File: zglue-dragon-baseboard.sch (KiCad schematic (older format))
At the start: 7 parts, among them U1 zGlue-Dragon

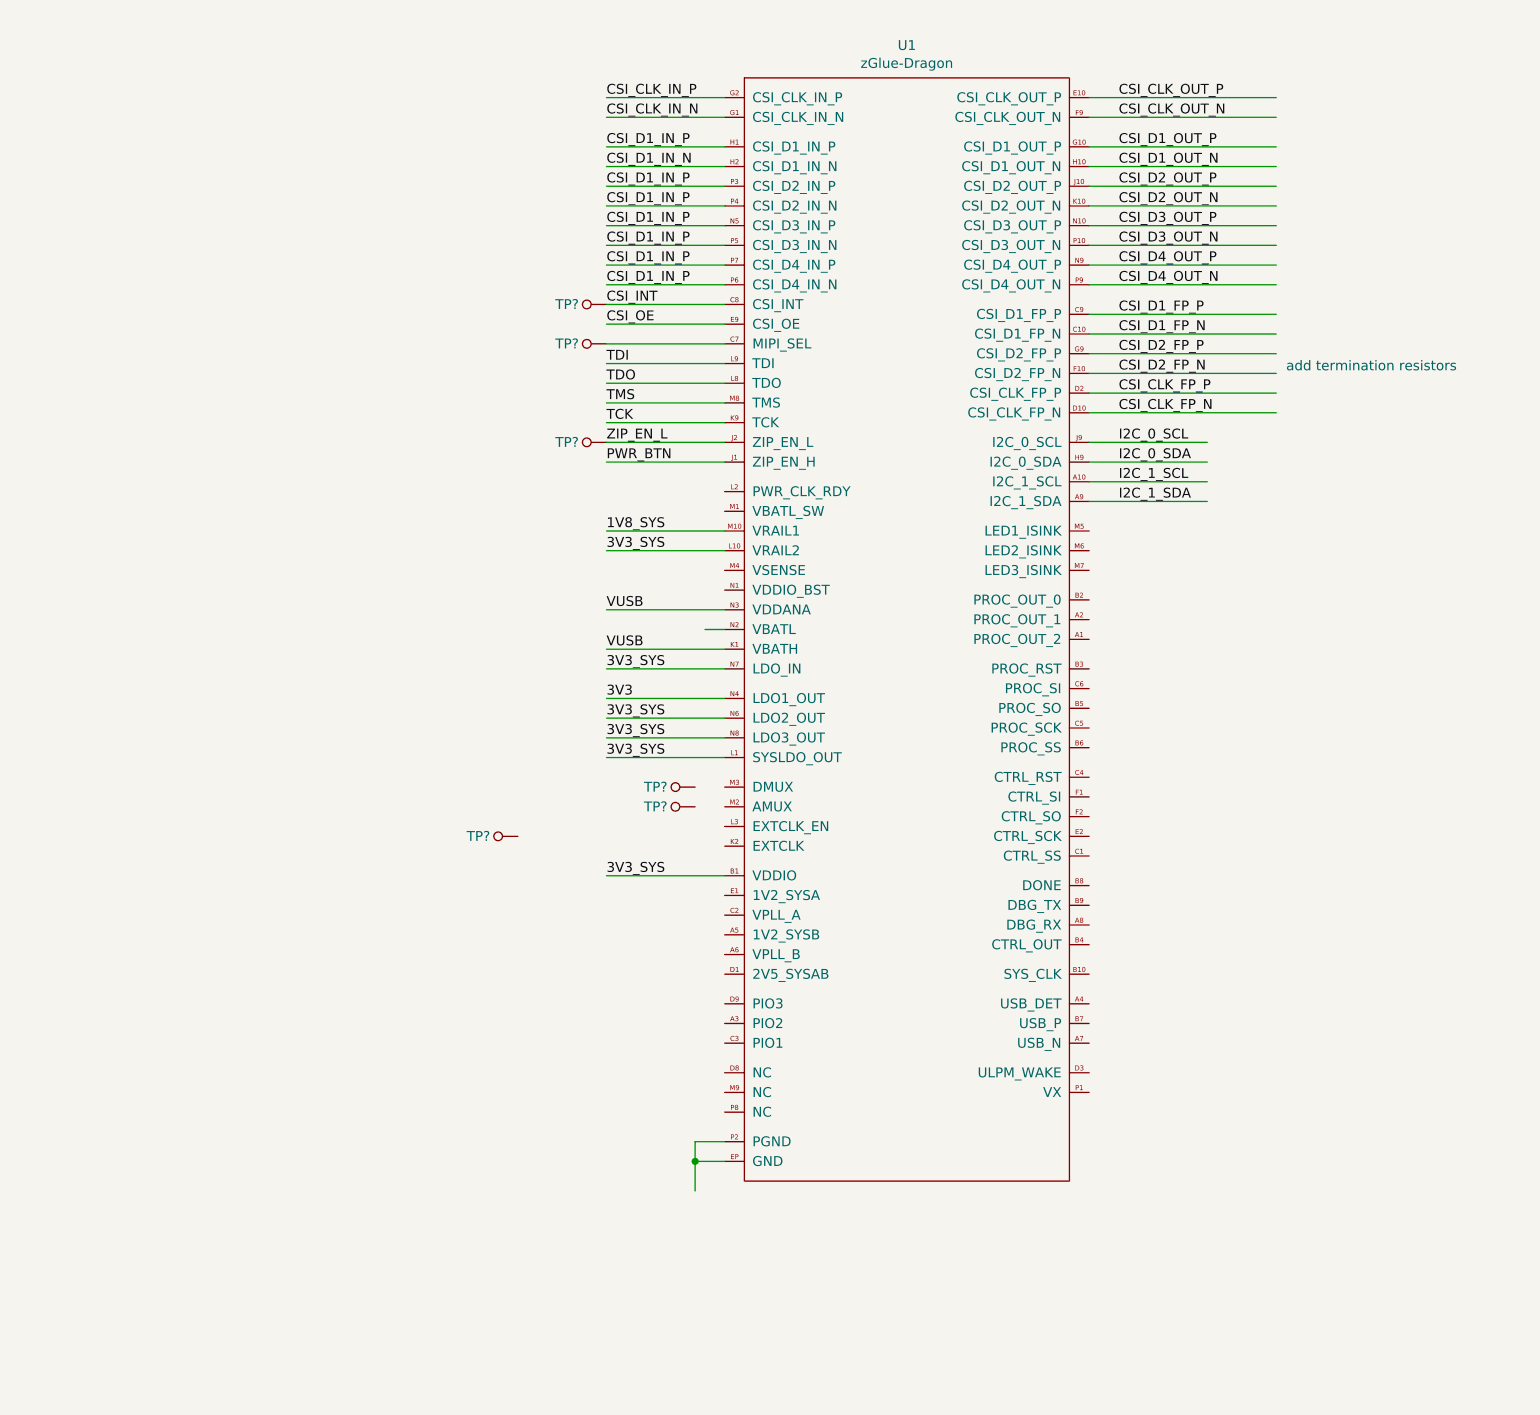
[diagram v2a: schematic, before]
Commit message: Added MIPI termination
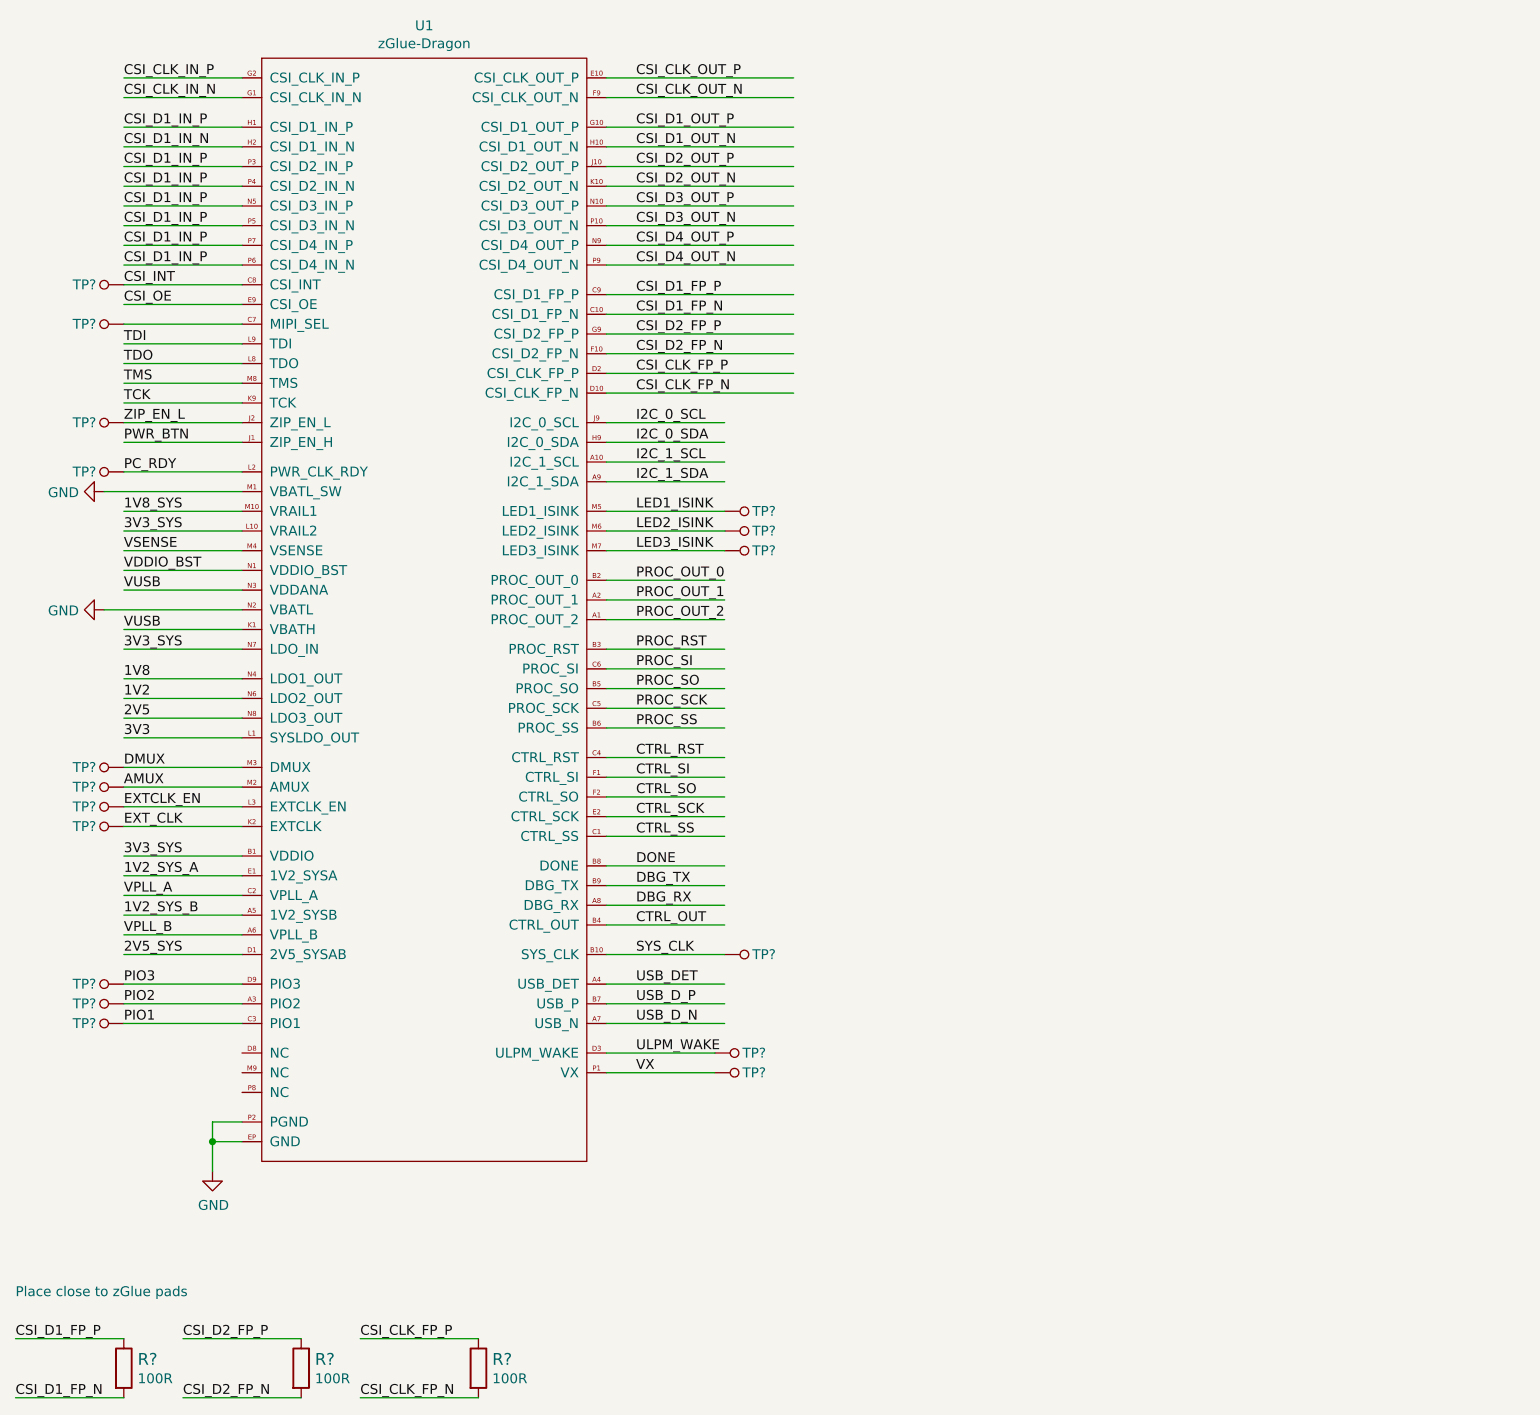
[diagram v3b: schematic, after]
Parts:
- added R? (x3): R_100R_0402, antmicro-footprints:0402-res, symbol antmicroResistors0402:R_100R_0402
- added TP? (x11): TP_SMD1MM, antmicro-footprints:Testpoint_smd_1mm, symbol antmicroTestPoints:TP_SMD1MM
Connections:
- net labels added: 1V2, 1V2_SYS_A, 1V2_SYS_B, 1V8, 2V5, 2V5_SYS, AMUX, CTRL_OUT, CTRL_RST, CTRL_SCK, CTRL_SI, CTRL_SO, CTRL_SS, DBG_RX, DBG_TX, DMUX, DONE, EXTCLK_EN, EXT_CLK, GND, LED1_ISINK, LED2_ISINK, LED3_ISINK, PC_RDY, PIO1, PIO2, PIO3, PROC_OUT_0, PROC_OUT_1, PROC_OUT_2, PROC_RST, PROC_SCK, PROC_SI, PROC_SO, PROC_SS, SYS_CLK, ULPM_WAKE, USB_DET, USB_D_N, USB_D_P, VDDIO_BST, VPLL_A, VPLL_B, VSENSE, VX
- wire segments 54 -> 102
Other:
- note added: "Place close to zGlue pads"
- note removed: "add termination resistors"
- moved on the sheet: TP?, U1

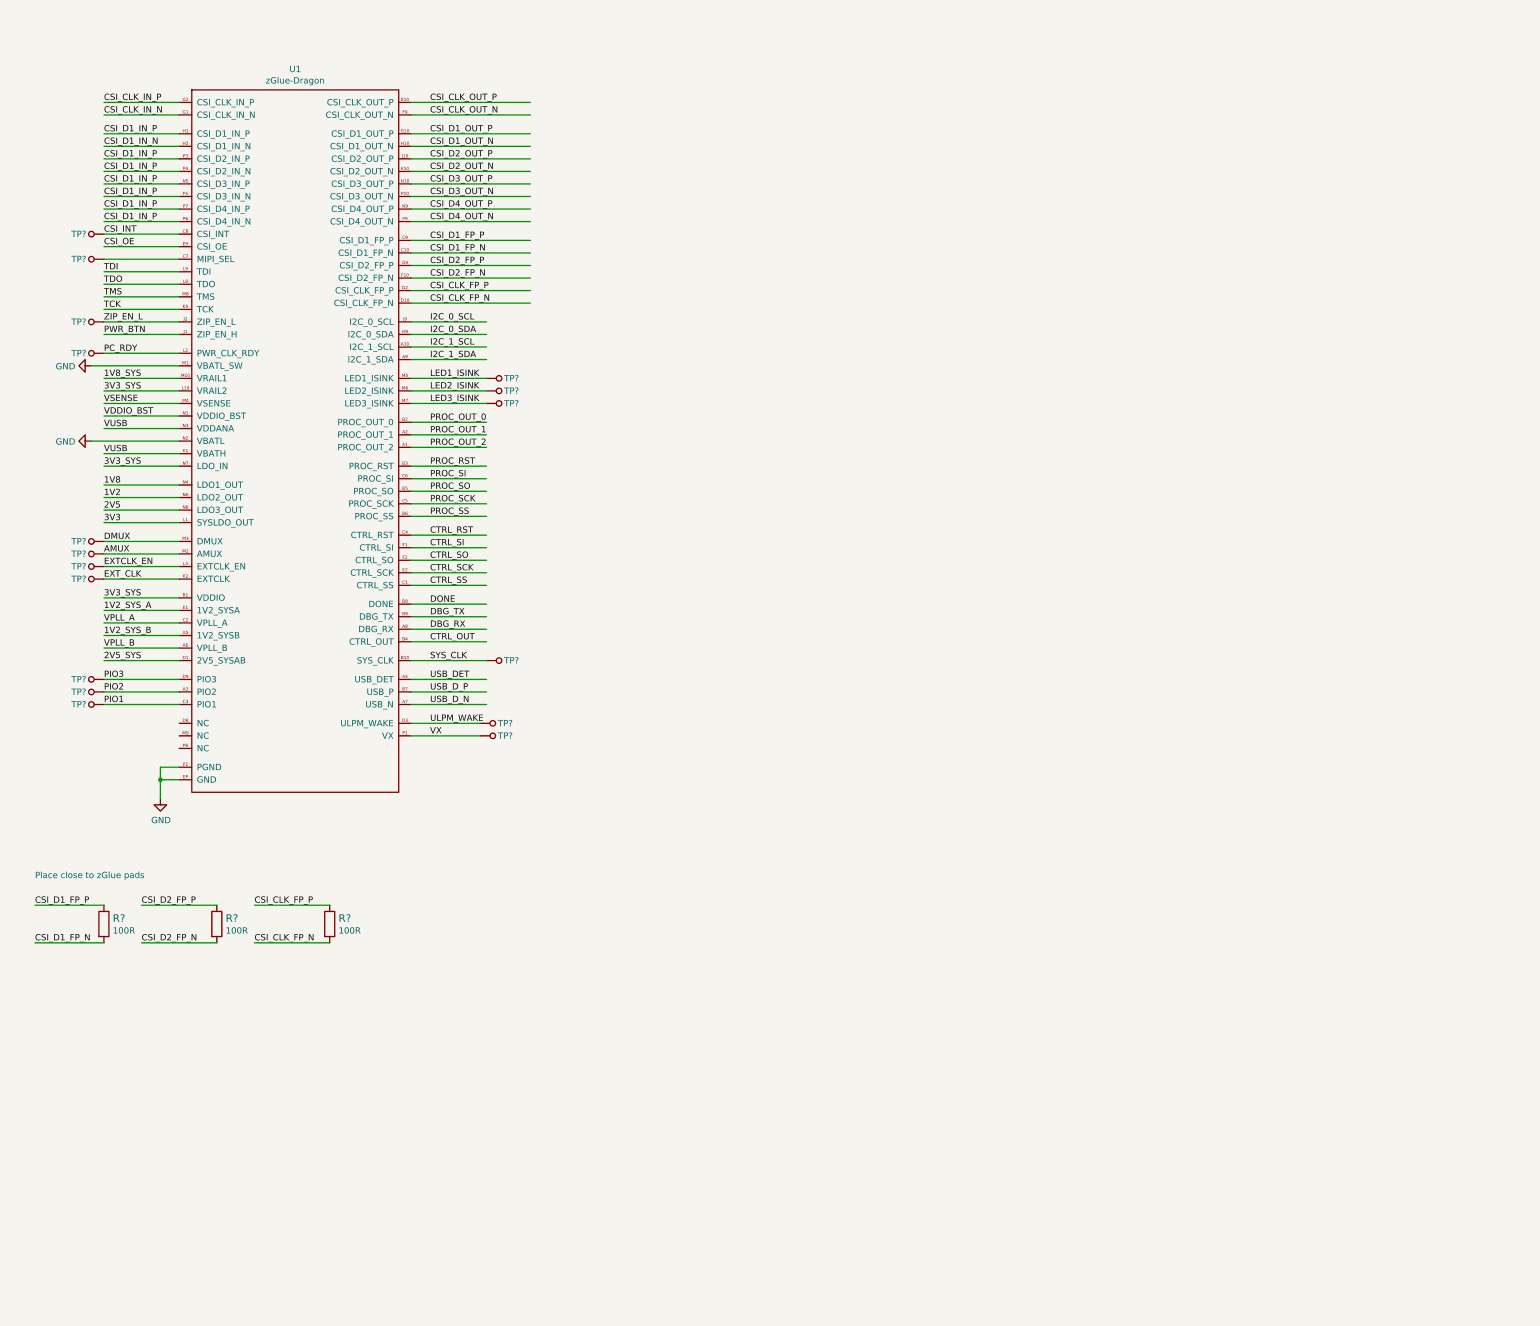
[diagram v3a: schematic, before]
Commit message: Added voltage filtering
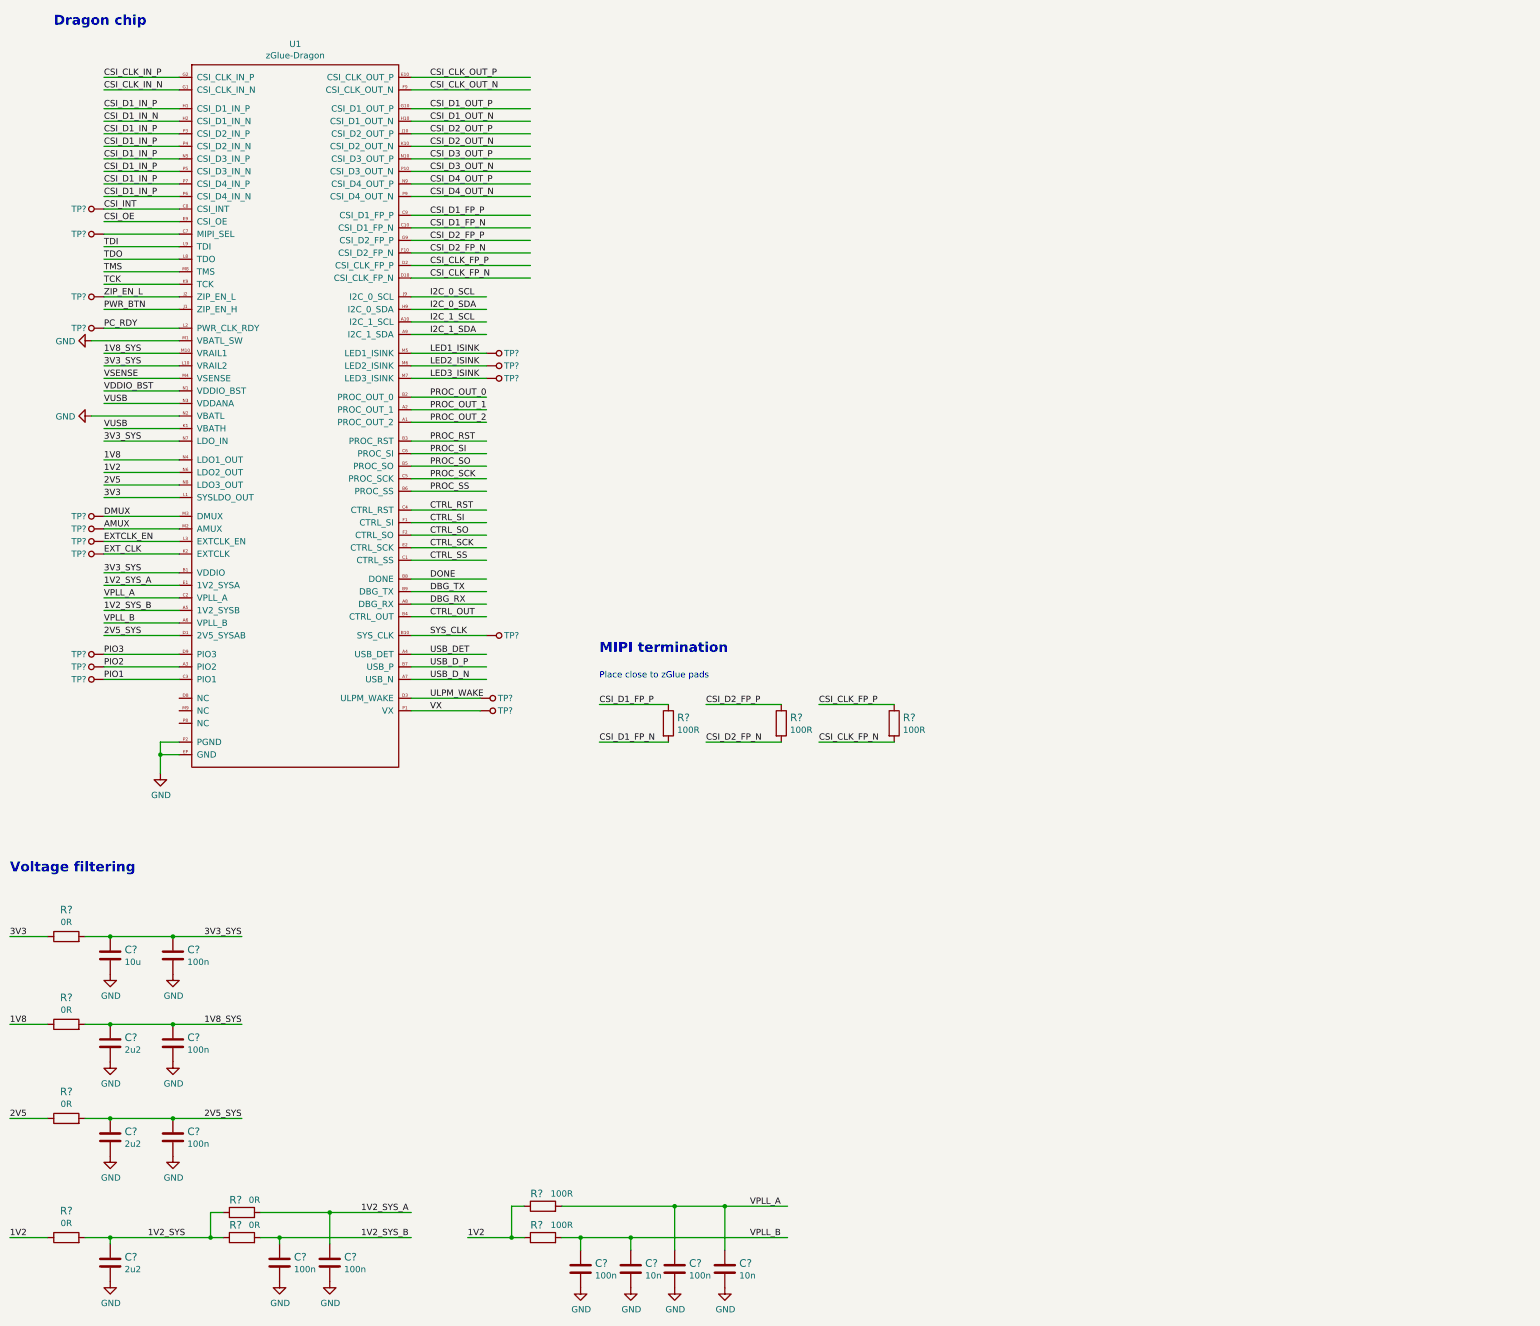
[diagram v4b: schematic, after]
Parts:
- added C?: C_10u_0402, antmicro-footprints:0402-cap, symbol antmicroCapacitors0402:C_10u_0402
- added C? (x7): C_100n_0402_6V3, antmicro-footprints:0402-cap, symbol antmicroCapacitors0402:C_100n_0402_6V3
- added C? (x3): C_2u2_0402, antmicro-footprints:0402-cap, symbol antmicroCapacitors0402:C_2u2_0402
- added C? (x2): C_10n_0402, antmicro-footprints:0402-cap, symbol antmicroCapacitors0402:C_10n_0402
- added R? (x6): R_0R_0402, antmicro-footprints:0402-res, symbol antmicroResistors0402:R_0R_0402
- added R? (x2): R_100R_0402, antmicro-footprints:0402-res, symbol antmicroResistors0402:R_100R_0402
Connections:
- net labels added: 1V2_SYS
- wire segments 102 -> 141
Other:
- note added: "Dragon chip"
- note added: "MIPI termination"
- note added: "Voltage filtering"
- moved on the sheet: R?, TP?, U1
